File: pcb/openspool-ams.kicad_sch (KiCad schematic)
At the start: 9 parts, among them J1 GND, J2 ESP32-L, J3 ESP32-R, J4 5V, J5 MOSI, J6 CS, J7 3V3, J8 SCK, J9 MISO

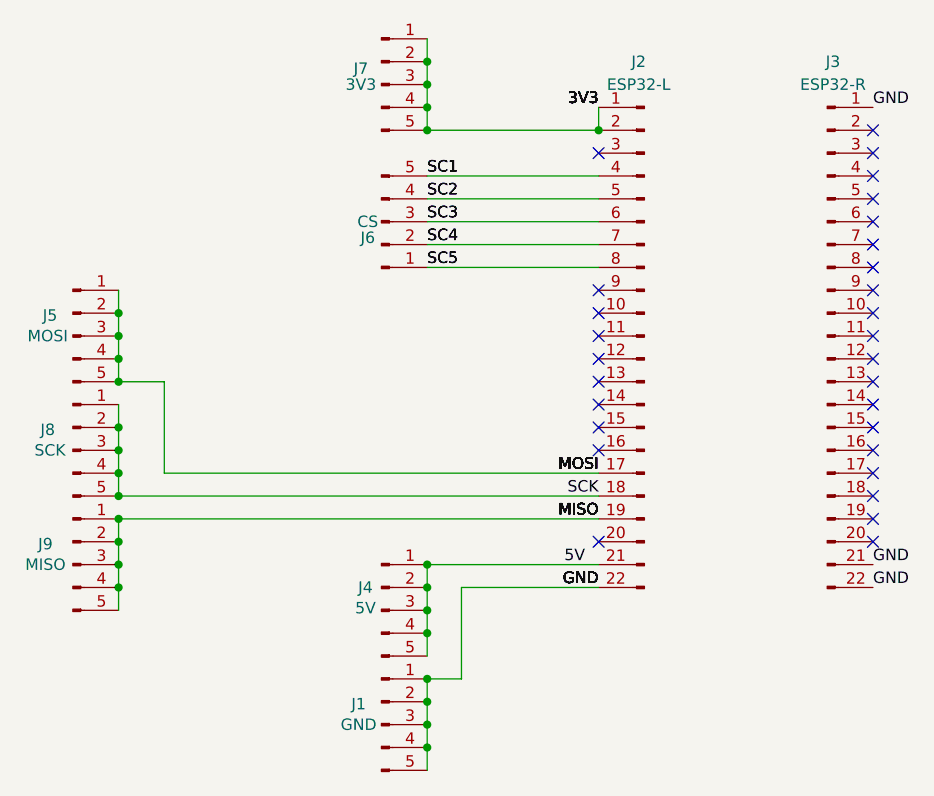
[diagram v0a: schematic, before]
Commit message: Added hints to silkscreen
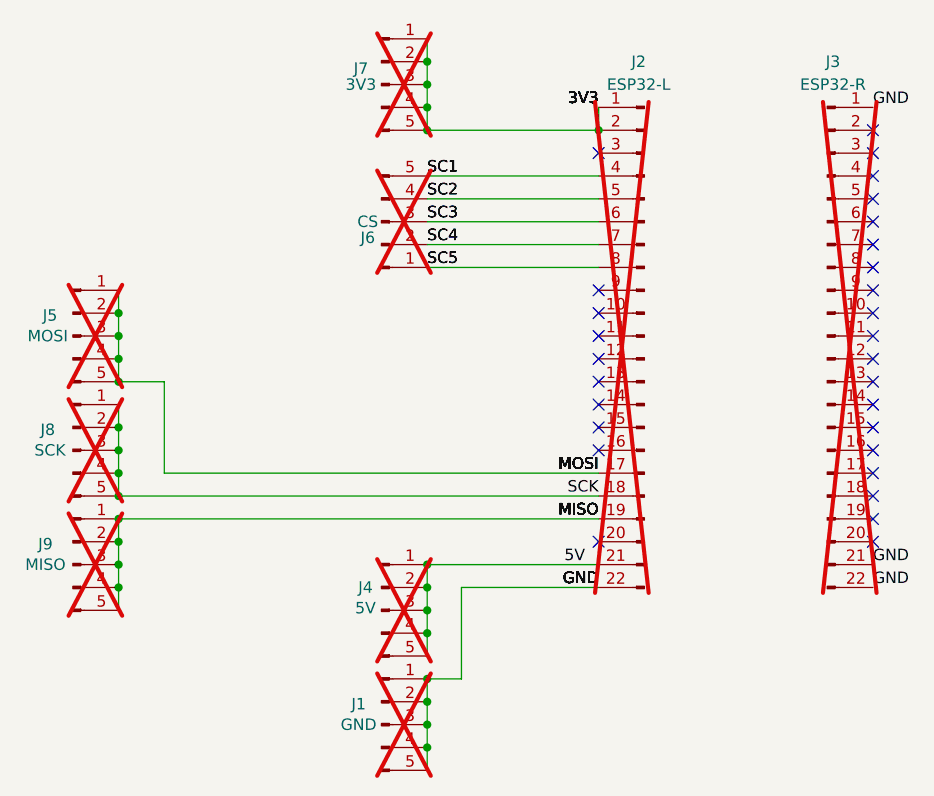
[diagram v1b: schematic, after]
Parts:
- J1, J2, J3, J4, J5, J6, J7, J8, J9: now not fitted
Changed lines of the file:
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@@
 		(in_bom yes)
 		(on_board yes)
-		(dnp no)
+		(dnp yes)
 		(property "Reference" "J7"
 			(at 58.674 52.832 0)
@@
 		(in_bom yes)
 		(on_board yes)
-		(dnp no)
+		(dnp yes)
 		(property "Reference" "J1"
 			(at 58.42 123.444 0)
@@
 		(in_bom yes)
 		(on_board yes)
-		(dnp no)
+		(dnp yes)
 		(property "Reference" "J6"
 			(at 59.436 71.628 0)
@@
 		(in_bom yes)
 		(on_board yes)
-		(dnp no)
+		(dnp yes)
 		(property "Reference" "J4"
 			(at 59.182 110.49 0)
@@
 		(in_bom yes)
 		(on_board yes)
-		(dnp no)
+		(dnp yes)
 		(fields_autoplaced yes)
 		(property "Reference" "J3"
@@
 		(in_bom yes)
 		(on_board yes)
-		(dnp no)
+		(dnp yes)
 		(property "Reference" "J2"
 			(at 89.535 52.07 0)
@@
 		(in_bom yes)
 		(on_board yes)
-		(dnp no)
+		(dnp yes)
 		(property "Reference" "J5"
 			(at 24.13 80.264 0)
@@
 		(in_bom yes)
 		(on_board yes)
-		(dnp no)
+		(dnp yes)
 		(property "Reference" "J8"
 			(at 23.876 92.964 0)
@@
 		(in_bom yes)
 		(on_board yes)
-		(dnp no)
+		(dnp yes)
 		(property "Reference" "J9"
 			(at 23.622 105.664 0)
